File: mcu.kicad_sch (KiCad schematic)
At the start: 12 parts, among them SW1 SW_Rotary_1x8_MP, U3 ESP32-DEVKITC-32UE

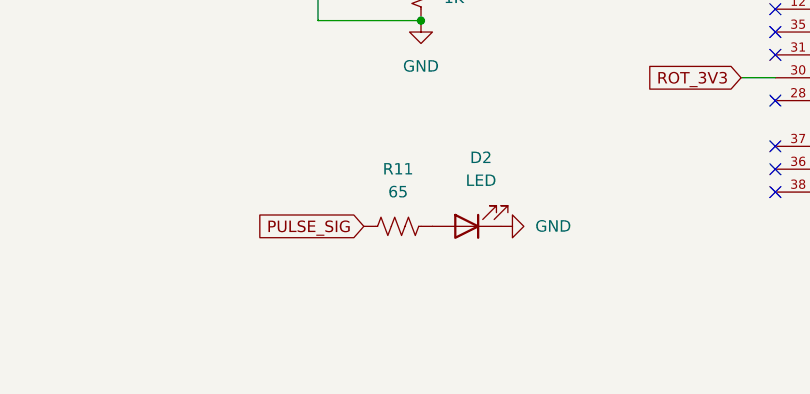
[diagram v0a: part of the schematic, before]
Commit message: routed PCB and added status LED for 5V
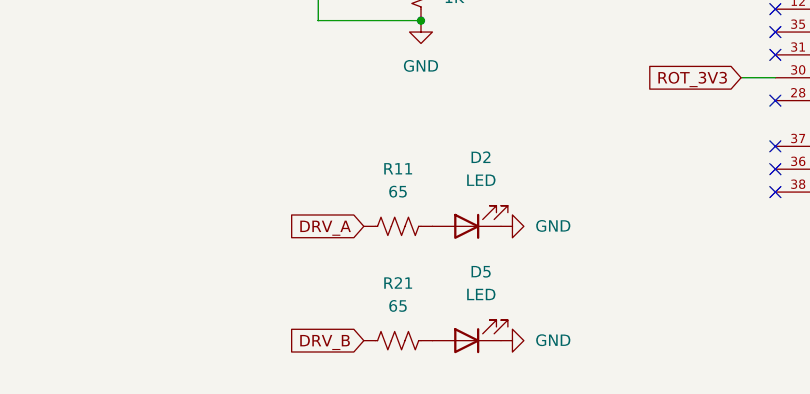
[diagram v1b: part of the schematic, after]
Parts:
- added D5: LED, LED_SMD:LED_0805_2012Metric_Pad1.15x1.40mm_HandSolder, symbol Device:LED
- added R21: 65, Resistor_SMD:R_0805_2012Metric_Pad1.20x1.40mm_HandSolder, symbol Device:R_US
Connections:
- net PULSE_SIG is gone; now on net DRV_A: R11.1
- net DRV_B: now also R21.1
- net GND: now also D5.1 (K)
- new net: D5.2 (A), R21.2
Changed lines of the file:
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@@
 		)
 	)
-	(global_label "PULSE_SIG"
+	(global_label "DRV_B"
 		(shape input)
-		(at 74.93 113.03 180)
+		(at 74.93 125.73 180)
 		(fields_autoplaced yes)
 		(effects
@@
 		)
 		(property "Intersheetrefs" "${INTERSHEET_REFS}"
-			(at 61.9058 113.03 0)
+			(at 66.0786 125.73 0)
+			(effects
+				(font
+					(size 1.27 1.27)
+				)
+				(justify right)
+				(hide yes)
+			)
+		)
+	)
+	(global_label "DRV_A"
+		(shape input)
+		(at 74.93 113.03 180)
+		(fields_autoplaced yes)
+		(effects
+			(font
+				(size 1.27 1.27)
+			)
+			(justify right)
+		)
+		(property "Intersheetrefs" "${INTERSHEET_REFS}"
+			(at 66.26 113.03 0)
 			(effects
 				(font
@@
 	)
 	(symbol
+		(lib_id "power:GND")
+		(at 90.17 125.73 90)
+		(unit 1)
+		(exclude_from_sim no)
+		(in_bom yes)
+		(on_board yes)
+		(dnp no)
+		(fields_autoplaced yes)
+		(property "Reference" "#PWR025"
+			(at 96.52 125.73 0)
+			(effects
+				(font
+					(size 1.27 1.27)
+				)
+				(hide yes)
+			)
+		)
+		(property "Value" "GND"
+			(at 93.98 125.7299 90)
+			(effects
+				(font
+					(size 1.27 1.27)
+				)
+				(justify right)
+			)
+		)
+		(property "Footprint" ""
+			(at 90.17 125.73 0)
+			(effects
+				(font
+					(size 1.27 1.27)
+				)
+				(hide yes)
+			)
+		)
+		(property "Datasheet" ""
+			(at 90.17 125.73 0)
+			(effects
+				(font
+					(size 1.27 1.27)
+				)
+				(hide yes)
+			)
+		)
+		(property "Description" "Power symbol creates a global label with name \"GND\" , ground"
+			(at 90.17 125.73 0)
+			(effects
+				(font
+					(size 1.27 1.27)
+				)
+				(hide yes)
+			)
+		)
+		(pin "1"
+		)
+		(instances
+			(project "FES_Hardware"
+				(path "/225cfa82-97e7-4320-90e1-4d94ef39f9f2/66e7fb16-fffa-4599-b9bd-167a6cbf40e4"
+					(reference "#PWR025")
+					(unit 1)
+				)
+			)
+		)
+	)
+	(symbol
 		(lib_id "Device:R_US")
 		(at 81.28 71.12 0)
@@
 	)
 	(symbol
+		(lib_id "Device:LED")
+		(at 86.36 125.73 180)
+		(unit 1)
+		(exclude_from_sim no)
+		(in_bom yes)
+		(on_board yes)
+		(dnp no)
+		(fields_autoplaced yes)
+		(property "Reference" "D5"
+			(at 87.9475 118.11 0)
+			(effects
+				(font
+					(size 1.27 1.27)
+				)
+			)
+		)
+		(property "Value" "LED"
+			(at 87.9475 120.65 0)
+			(effects
+				(font
+					(size 1.27 1.27)
+				)
+			)
+		)
+		(property "Footprint" "LED_SMD:LED_0805_2012Metric_Pad1.15x1.40mm_HandSolder"
+			(at 86.36 125.73 0)
+			(effects
+				(font
+					(size 1.27 1.27)
+				)
+				(hide yes)
+			)
+		)
+		(property "Datasheet" "~"
+			(at 86.36 125.73 0)
+			(effects
+				(font
+					(size 1.27 1.27)
+				)
+				(hide yes)
+			)
+		)
+		(property "Description" "Light emitting diode"
+			(at 86.36 125.73 0)
+			(effects
+				(font
+					(size 1.27 1.27)
+				)
+				(hide yes)
+			)
+		)
+		(pin "2"
+		)
+		(pin "1"
+		)
+		(instances
+			(project "FES_Hardware"
+				(path "/225cfa82-97e7-4320-90e1-4d94ef39f9f2/66e7fb16-fffa-4599-b9bd-167a6cbf40e4"
+					(reference "D5")
+					(unit 1)
+				)
+			)
+		)
+	)
+	(symbol
 		(lib_id "power:GND")
 		(at 90.17 113.03 90)
@@
 					(unit 1)
 				)
+			)
+		)
+	)
+	(symbol
+		(lib_id "Device:R_US")
+		(at 78.74 125.73 90)
+		(unit 1)
+		(exclude_from_sim no)
+		(in_bom yes)
+		(on_board yes)
+		(dnp no)
+		(fields_autoplaced yes)
+		(property "Reference" "R21"
+			(at 78.74 119.38 90)
+			(effects
+				(font
+					(size 1.27 1.27)
+				)
+			)
+		)
+		(property "Value" "65"
+			(at 78.74 121.92 90)
+			(effects
+				(font
+					(size 1.27 1.27)
+				)
+			)
+		)
+		(property "Footprint" "Resistor_SMD:R_0805_2012Metric_Pad1.20x1.40mm_HandSolder"
+			(at 78.994 124.714 90)
+			(effects
+				(font
+					(size 1.27 1.27)
+				)
+				(hide yes)
+			)
+		)
+		(property "Datasheet" "~"
+			(at 78.74 125.73 0)
+			(effects
+				(font
+					(size 1.27 1.27)
+				)
+				(hide yes)
+			)
+		)
+		(property "Description" "Resistor, US symbol"
+			(at 78.74 125.73 0)
+			(effects
+				(font
+					(size 1.27 1.27)
+				)
+				(hide yes)
+			)
+		)
+		(pin "1"
+		)
+		(pin "2"
+		)
+		(instances
+			(project "FES_Hardware"
+				(path "/225cfa82-97e7-4320-90e1-4d94ef39f9f2/66e7fb16-fffa-4599-b9bd-167a6cbf40e4"
+					(reference "R21")
+					(unit 1)
+				)

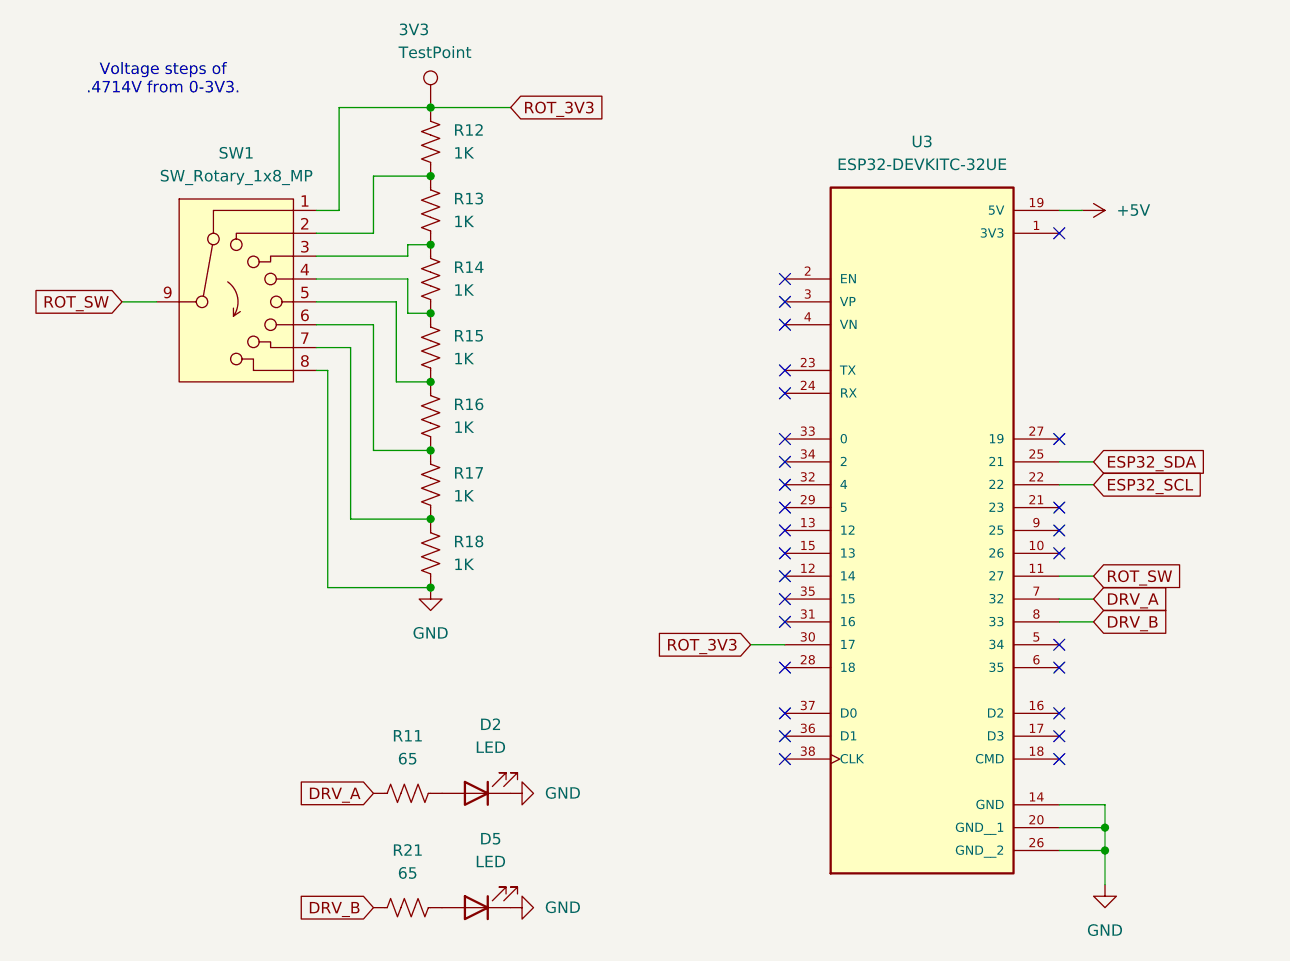
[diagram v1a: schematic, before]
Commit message: tidied up PCB routing, renamed HV_OUT, changed MCU footprint/schematic
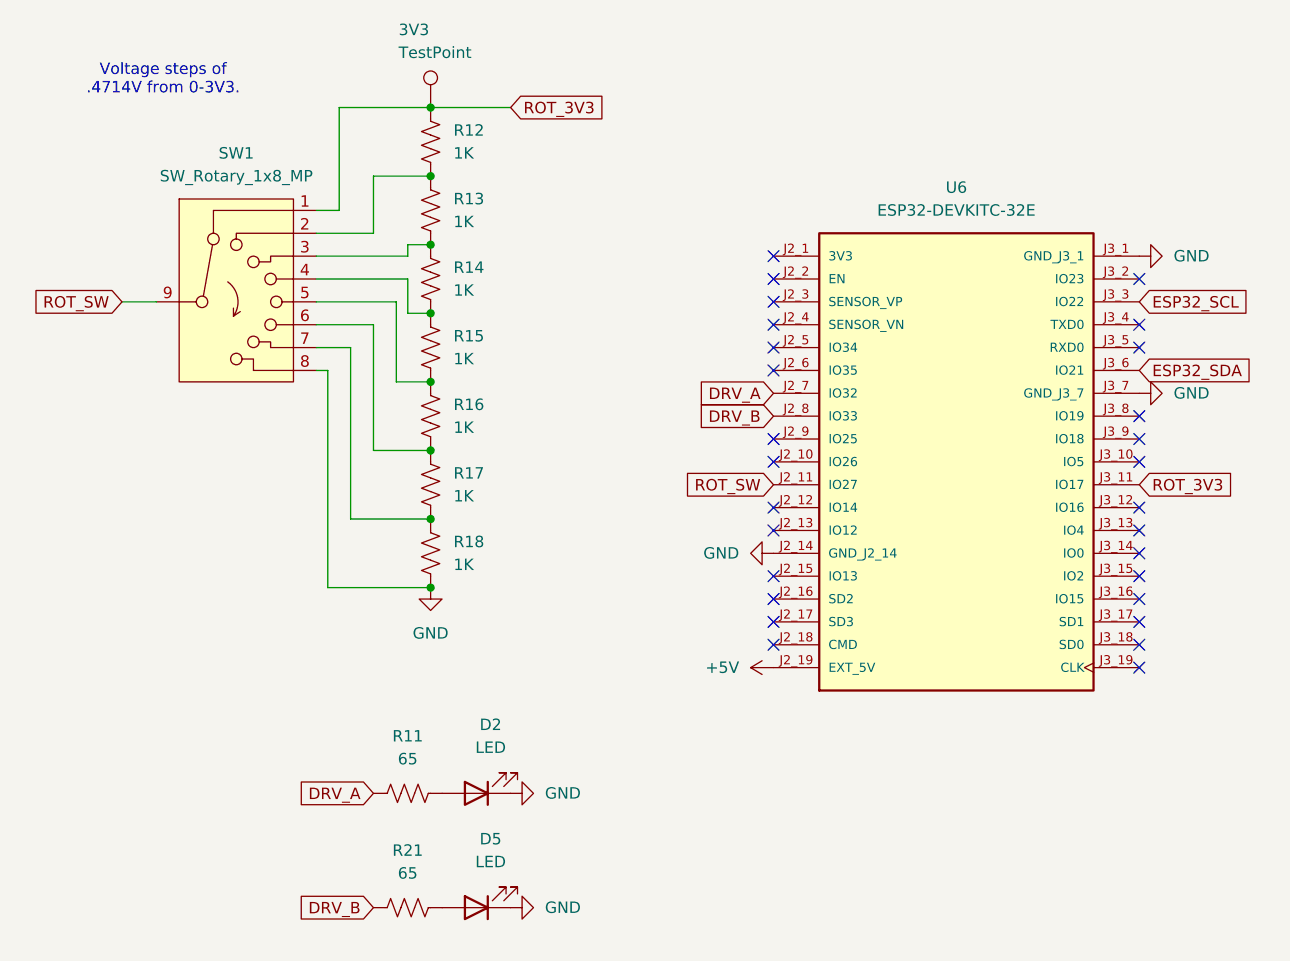
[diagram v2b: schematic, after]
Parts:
- removed U3: ESP32-DEVKITC-32UE, ESP32-DEVKITC_32UE:ESPRESSIF_ESP32-DEVKITC-32UE, symbol ESP32-DEVKITC-32UE:ESP32-DEVKITC-32UE
- added U6: ESP32-DEVKITC-32E, ESP32-DEVKITC-32E:MODULE_ESP32-DEVKITC-32E, symbol ESP32-DEVKITC-32E:ESP32-DEVKITC-32E
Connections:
- net +5V: now also U6.J2_19 (EXT_5V)
- net DRV_A: now also U6.J2_7 (IO32)
- net DRV_B: now also U6.J2_8 (IO33)
- net ESP32_SCL: now also U6.J3_3 (IO22)
- net ESP32_SDA: now also U6.J3_6 (IO21)
- net GND: now also U6.J2_14 (GND_J2_14), U6.J3_1 (GND_J3_1), U6.J3_7 (GND_J3_7)
- net ROT_3V3: now also U6.J3_11 (IO17)
- net ROT_SW: now also U6.J2_11 (IO27)

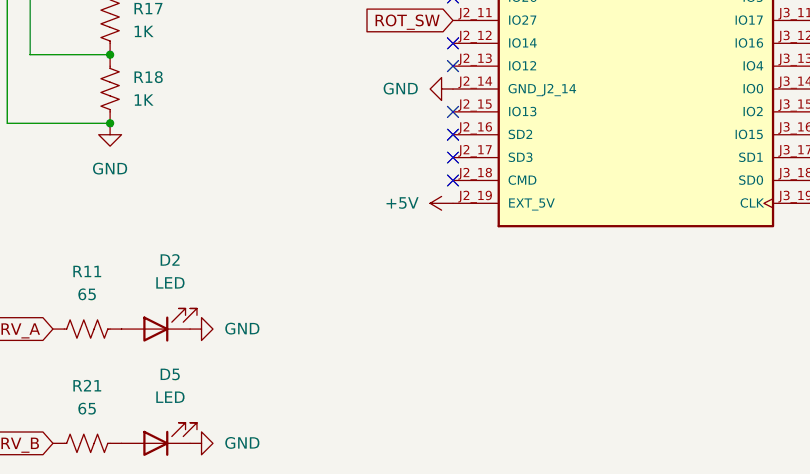
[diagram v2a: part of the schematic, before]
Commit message: added decoupling caps to MCU 5V input
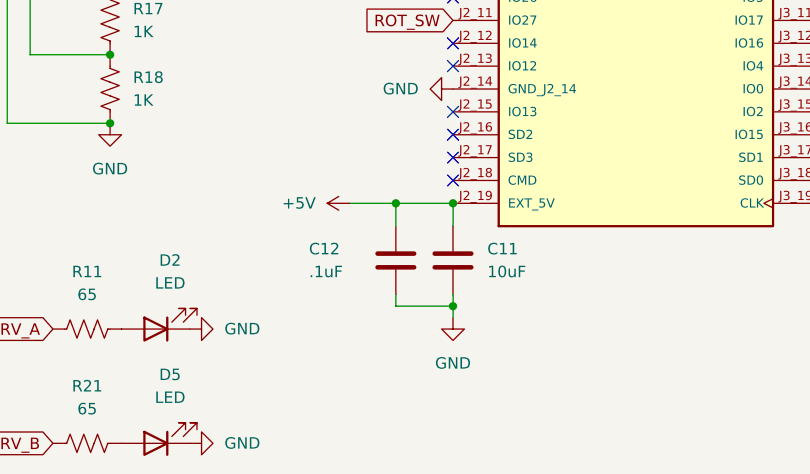
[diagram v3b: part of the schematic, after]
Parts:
- added C11: 10uF, Capacitor_SMD:C_0805_2012Metric_Pad1.18x1.45mm_HandSolder, symbol Device:C
- added C12: .1uF, Capacitor_SMD:C_0805_2012Metric_Pad1.18x1.45mm_HandSolder, symbol Device:C
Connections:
- net +5V: now also C11.1, C12.1
- net GND: now also C11.2, C12.2
